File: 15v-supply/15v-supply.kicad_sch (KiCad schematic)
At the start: 29 parts, among them J901 Terminal Block, J902 Terminal Block, P901 120VAC, SW901 SW_SPST, T901 XFORMER, U901 LM7815, U902 LM7915

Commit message: if and log amp routing and 3d model
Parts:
- C901: value (none) -> 0.22u; footprint (none) -> Capacitor_THT:C_Rect_L4.6mm_W5.5mm_P2.50mm_MKS02_FKP02
- D901, D902, D903, D904: Spice_Lib_File 15v-supply-spice\1n5060.lib -> 15v-supply-spice/1n5060.lib
- H901, H902, H903, H905: Spice_Netlist_Enabled (none) -> N; Spice_Primitive (none) -> R
- R901, R902: value (none) -> 2.2k; footprint (none) -> Resistor_THT:R_Axial_DIN0309_L9.0mm_D3.2mm_P12.70mm_Horizontal
- T901: Spice_Lib_File 15v-supply-spice\xformer.lib -> 15v-supply-spice/xformer.lib
- U901, U902: Spice_Lib_File 15v-supply-spice\regulators.lib -> 15v-supply-spice/regulators.lib
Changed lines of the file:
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@@
     (title "Dual Polarity 15V Supply")
     (date "2022-06-16")
-    (rev "0.1")
+    (rev "0.0")
     (company "Andy McCann KA3KAF and Doug McCann KA3KAG")
     (comment 2 "Audiophile's Project Source Book, Fig 7-8")
@@
       (effects (font (size 1.27 1.27)) (justify left))
     )
-    (property "Value" "" (id 1) (at 127 120.6499 0)
-      (effects (font (size 1.27 1.27)) (justify left))
-    )
-    (property "Footprint" "" (id 2) (at 124.46 119.38 0)
+    (property "Value" "2.2k" (id 1) (at 127 120.6499 0)
+      (effects (font (size 1.27 1.27)) (justify left))
+    )
+    (property "Footprint" "Resistor_THT:R_Axial_DIN0309_L9.0mm_D3.2mm_P12.70mm_Horizontal" (id 2) (at 124.46 119.38 0)
       (effects (font (size 1.27 1.27)) hide)
     )
@@
       (effects (font (size 1.27 1.27)) hide)
     )
+    (property "Spice_Primitive" "R" (id 4) (at 39.37 196.85 0)
+      (effects (font (size 1.27 1.27)) hide)
+    )
+    (property "Spice_Netlist_Enabled" "N" (id 5) (at 39.37 196.85 0)
+      (effects (font (size 1.27 1.27)) hide)
+    )
   )
   (symbol (lib_id "Device:C_Small") (at 158.75 40.64 0) (unit 1)
@@
     )
     (property "Datasheet" "~" (id 3) (at 76.2 196.85 0)
+      (effects (font (size 1.27 1.27)) hide)
+    )
+    (property "Spice_Primitive" "R" (id 4) (at 76.2 196.85 0)
+      (effects (font (size 1.27 1.27)) hide)
+    )
+    (property "Spice_Netlist_Enabled" "N" (id 5) (at 76.2 196.85 0)
       (effects (font (size 1.27 1.27)) hide)
     )
@@
       (effects (font (size 1.27 1.27)) hide)
     )
-    (property "Spice_Lib_File" "15v-supply-spice\\1n5060.lib" (id 8) (at 177.8 40.64 0)
+    (property "Spice_Lib_File" "15v-supply-spice/1n5060.lib" (id 8) (at 177.8 40.64 0)
       (effects (font (size 1.27 1.27)) hide)
     )
@@
       (effects (font (size 1.27 1.27)) hide)
     )
-    (property "Spice_Lib_File" "15v-supply-spice\\1n5060.lib" (id 8) (at 140.97 74.93 0)
+    (property "Spice_Lib_File" "15v-supply-spice/1n5060.lib" (id 8) (at 140.97 74.93 0)
       (effects (font (size 1.27 1.27)) hide)
     )
@@
       (effects (font (size 1.27 1.27)) (justify left))
     )
-    (property "Value" "" (id 1) (at 127 152.3999 0)
-      (effects (font (size 1.27 1.27)) (justify left))
-    )
-    (property "Footprint" "" (id 2) (at 124.46 151.13 0)
+    (property "Value" "2.2k" (id 1) (at 127 152.3999 0)
+      (effects (font (size 1.27 1.27)) (justify left))
+    )
+    (property "Footprint" "Resistor_THT:R_Axial_DIN0309_L9.0mm_D3.2mm_P12.70mm_Horizontal" (id 2) (at 124.46 151.13 0)
       (effects (font (size 1.27 1.27)) hide)
     )
@@
       (effects (font (size 1.27 1.27)) hide)
     )
-    (property "Spice_Lib_File" "15v-supply-spice\\xformer.lib" (id 7) (at 87.63 54.61 0)
+    (property "Spice_Lib_File" "15v-supply-spice/xformer.lib" (id 7) (at 87.63 54.61 0)
       (effects (font (size 1.27 1.27)) hide)
     )
@@
       (effects (font (size 1.27 1.27)) hide)
     )
-    (property "Spice_Lib_File" "15v-supply-spice\\1n5060.lib" (id 8) (at 177.8 74.93 0)
+    (property "Spice_Lib_File" "15v-supply-spice/1n5060.lib" (id 8) (at 177.8 74.93 0)
       (effects (font (size 1.27 1.27)) hide)
     )
@@
       (effects (font (size 1.27 1.27)) hide)
     )
+    (property "Spice_Primitive" "R" (id 4) (at 20.32 196.85 0)
+      (effects (font (size 1.27 1.27)) hide)
+    )
+    (property "Spice_Netlist_Enabled" "N" (id 5) (at 20.32 196.85 0)
+      (effects (font (size 1.27 1.27)) hide)
+    )
   )
   (symbol (lib_id "terminal-block:691103110003") (at 121.92 54.61 270) (unit 1)
@@
       (effects (font (size 1.27 1.27)) hide)
     )
-    (property "Spice_Lib_File" "15v-supply-spice\\1n5060.lib" (id 7) (at 140.97 40.64 0)
+    (property "Spice_Lib_File" "15v-supply-spice/1n5060.lib" (id 7) (at 140.97 40.64 0)
       (effects (font (size 1.27 1.27)) hide)
     )
@@
       (effects (font (size 1.27 1.27)) hide)
     )
-    (property "Spice_Lib_File" "15v-supply-spice\\regulators.lib" (id 8) (at 76.2 109.22 0)
+    (property "Spice_Lib_File" "15v-supply-spice/regulators.lib" (id 8) (at 76.2 109.22 0)
       (effects (font (size 1.27 1.27)) hide)
     )
@@
       (effects (font (size 1.27 1.27)) (justify left))
     )
-    (property "Value" "" (id 1) (at 69.85 55.8799 0)
-      (effects (font (size 1.27 1.27)) (justify left))
-    )
-    (property "Footprint" "" (id 2) (at 66.04 54.61 0)
+    (property "Value" "0.22u" (id 1) (at 69.85 55.8799 0)
+      (effects (font (size 1.27 1.27)) (justify left))
+    )
+    (property "Footprint" "Capacitor_THT:C_Rect_L4.6mm_W5.5mm_P2.50mm_MKS02_FKP02" (id 2) (at 66.04 54.61 0)
       (effects (font (size 1.27 1.27)) hide)
     )
@@
       (effects (font (size 1.27 1.27)) hide)
     )
-    (property "Spice_Lib_File" "15v-supply-spice\\regulators.lib" (id 8) (at 76.2 161.29 0)
+    (property "Spice_Lib_File" "15v-supply-spice/regulators.lib" (id 8) (at 76.2 161.29 0)
       (effects (font (size 1.27 1.27)) hide)
     )
@@
       (effects (font (size 1.27 1.27)) hide)
     )
+    (property "Spice_Primitive" "R" (id 4) (at 58.42 196.85 0)
+      (effects (font (size 1.27 1.27)) hide)
+    )
+    (property "Spice_Netlist_Enabled" "N" (id 5) (at 58.42 196.85 0)
+      (effects (font (size 1.27 1.27)) hide)
+    )

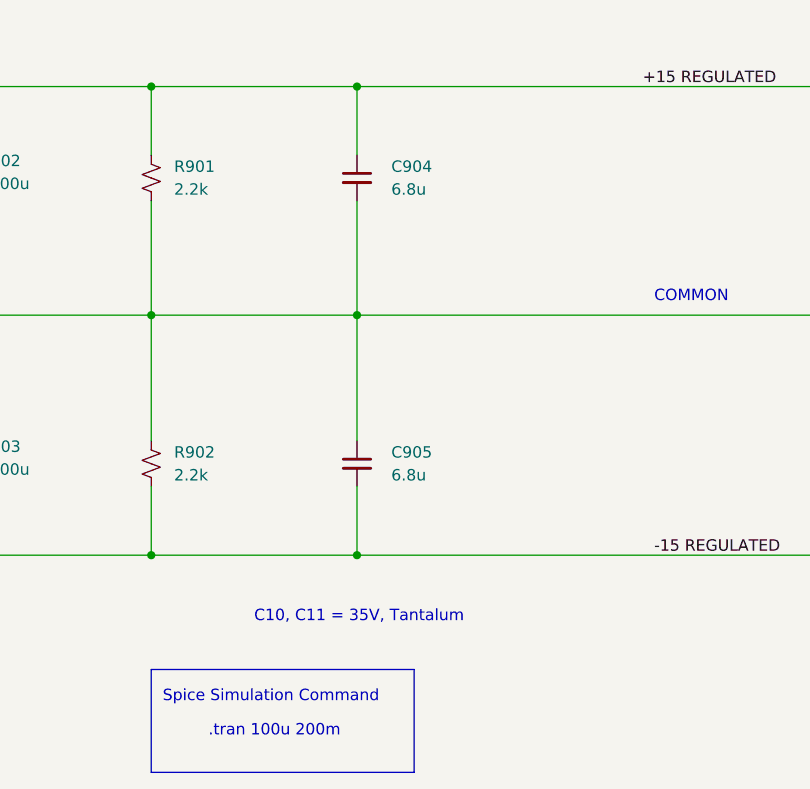
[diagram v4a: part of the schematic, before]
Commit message: Improvements to if and log amp
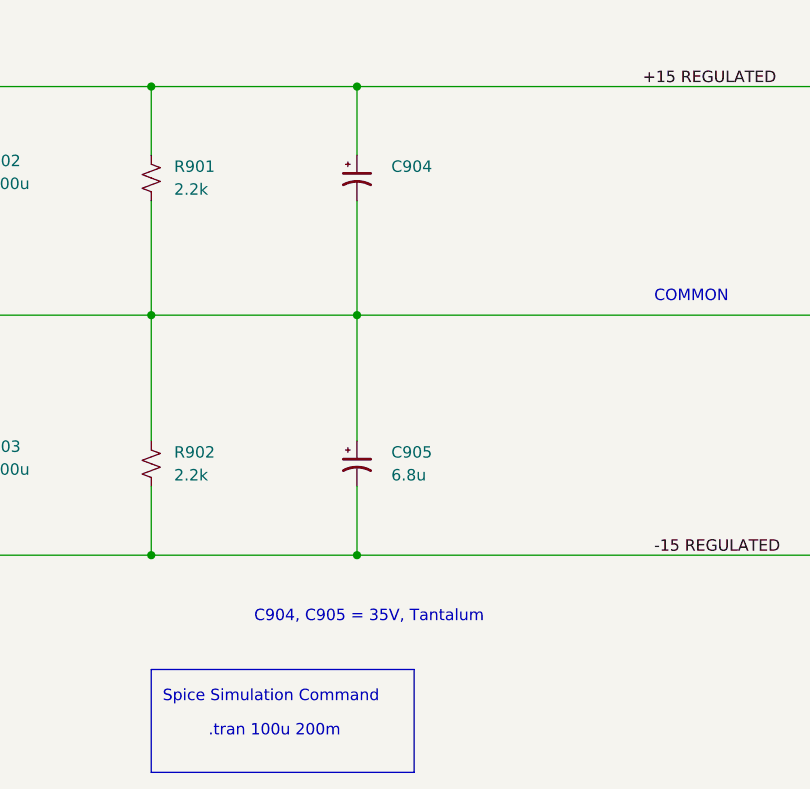
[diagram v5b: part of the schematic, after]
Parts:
- C904: value 6.8u -> (none); footprint Capacitor_THT:CP_Radial_D5.0mm_P2.50mm -> (none); symbol Device:C_Small -> Device:C_Polarized_Small_US
- C905: symbol Device:C_Small -> Device:C_Polarized_Small_US
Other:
- note added: "C904, C905 = 35V, Tantalum"
- note removed: "C10, C11 = 35V, Tantalum"
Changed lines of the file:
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@@
     (effects (font (size 1.27 1.27)) (justify left bottom))
   )
-  (text "C10, C11 = 35V, Tantalum" (at 135.89 168.91 0)
+  (text "C904, C905 = 35V, Tantalum" (at 135.89 168.91 0)
     (effects (font (size 1.27 1.27)) (justify left bottom))
   )
@@
     (pin "2")
   )
-  (symbol (lib_id "Device:C_Small") (at 147.32 151.13 0) (unit 1)
+  (symbol (lib_id "Device:C_Polarized_Small_US") (at 147.32 151.13 0) (unit 1)
     (in_bom yes) (on_board yes) (fields_autoplaced)
     (property "Reference" "C905" (id 0) (at 151.13 149.8599 0)
@@
       (effects (font (size 1.27 1.27)) hide)
     )
-    (property "Datasheet" "https://datasheets.kyocera-avx.com/tap.pdf" (id 3) (at 147.32 151.13 0)
-      (effects (font (size 1.27 1.27)) hide)
-    )
-    (pin "1")
-    (pin "2")
-  )
-  (symbol (lib_id "Device:C_Small") (at 147.32 119.38 0) (unit 1)
+    (property "Datasheet" "~" (id 3) (at 147.32 151.13 0)
+      (effects (font (size 1.27 1.27)) hide)
+    )
+    (pin "1")
+    (pin "2")
+  )
+  (symbol (lib_id "Device:C_Polarized_Small_US") (at 147.32 119.38 0) (unit 1)
     (in_bom yes) (on_board yes) (fields_autoplaced)
     (property "Reference" "C904" (id 0) (at 151.13 118.1099 0)
       (effects (font (size 1.27 1.27)) (justify left))
     )
-    (property "Value" "6.8u" (id 1) (at 151.13 120.6499 0)
-      (effects (font (size 1.27 1.27)) (justify left))
-    )
-    (property "Footprint" "Capacitor_THT:CP_Radial_D5.0mm_P2.50mm" (id 2) (at 147.32 119.38 0)
-      (effects (font (size 1.27 1.27)) hide)
-    )
-    (property "Datasheet" "https://datasheets.kyocera-avx.com/tap.pdf" (id 3) (at 147.32 119.38 0)
-      (effects (font (size 1.27 1.27)) hide)
-    )
+    (property "Value" "" (id 1) (at 151.13 120.6499 0)
+      (effects (font (size 1.27 1.27)) (justify left))
+    )
+    (property "Footprint" "" (id 2) (at 147.32 119.38 0)
+      (effects (font (size 1.27 1.27)) hide)
+    )
+    (property "Datasheet" "~" (id 3) (at 147.32 119.38 0)
+      (effects (font (size 1.27 1.27)) hide)
+    )

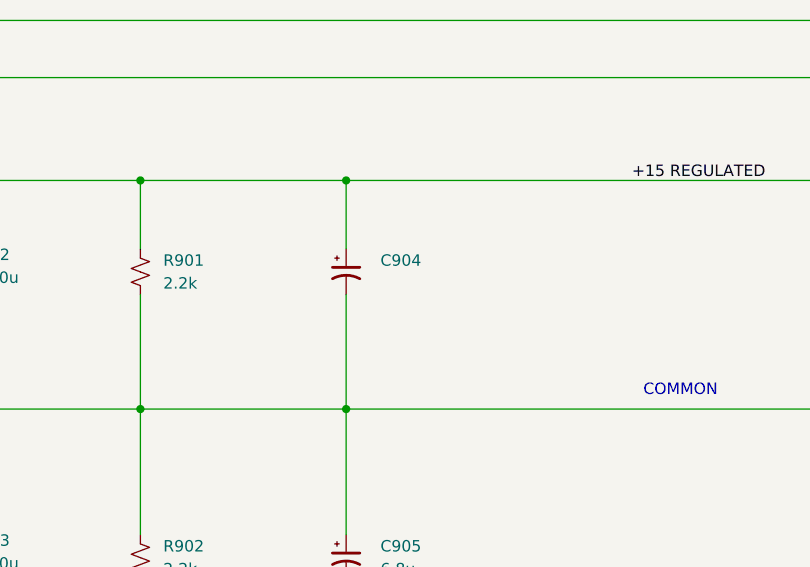
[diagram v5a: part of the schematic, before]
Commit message: updates to 15v supply and if and log amp boards so boards can be sent to fab
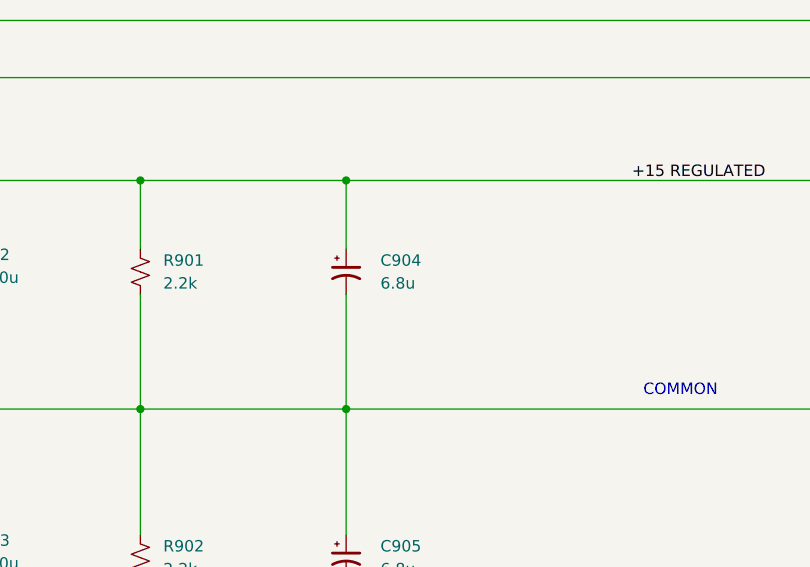
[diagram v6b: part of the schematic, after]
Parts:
- C904: value (none) -> 6.8u; footprint (none) -> Capacitor_THT:CP_Radial_D5.0mm_P2.50mm
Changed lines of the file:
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@@
       (effects (font (size 1.27 1.27)) (justify left))
     )
-    (property "Value" "" (id 1) (at 151.13 120.6499 0)
+    (property "Value" "6.8u" (id 1) (at 151.13 120.6499 0)
       (effects (font (size 1.27 1.27)) (justify left))
     )
-    (property "Footprint" "" (id 2) (at 147.32 119.38 0)
+    (property "Footprint" "Capacitor_THT:CP_Radial_D5.0mm_P2.50mm" (id 2) (at 147.32 119.38 0)
       (effects (font (size 1.27 1.27)) hide)
     )

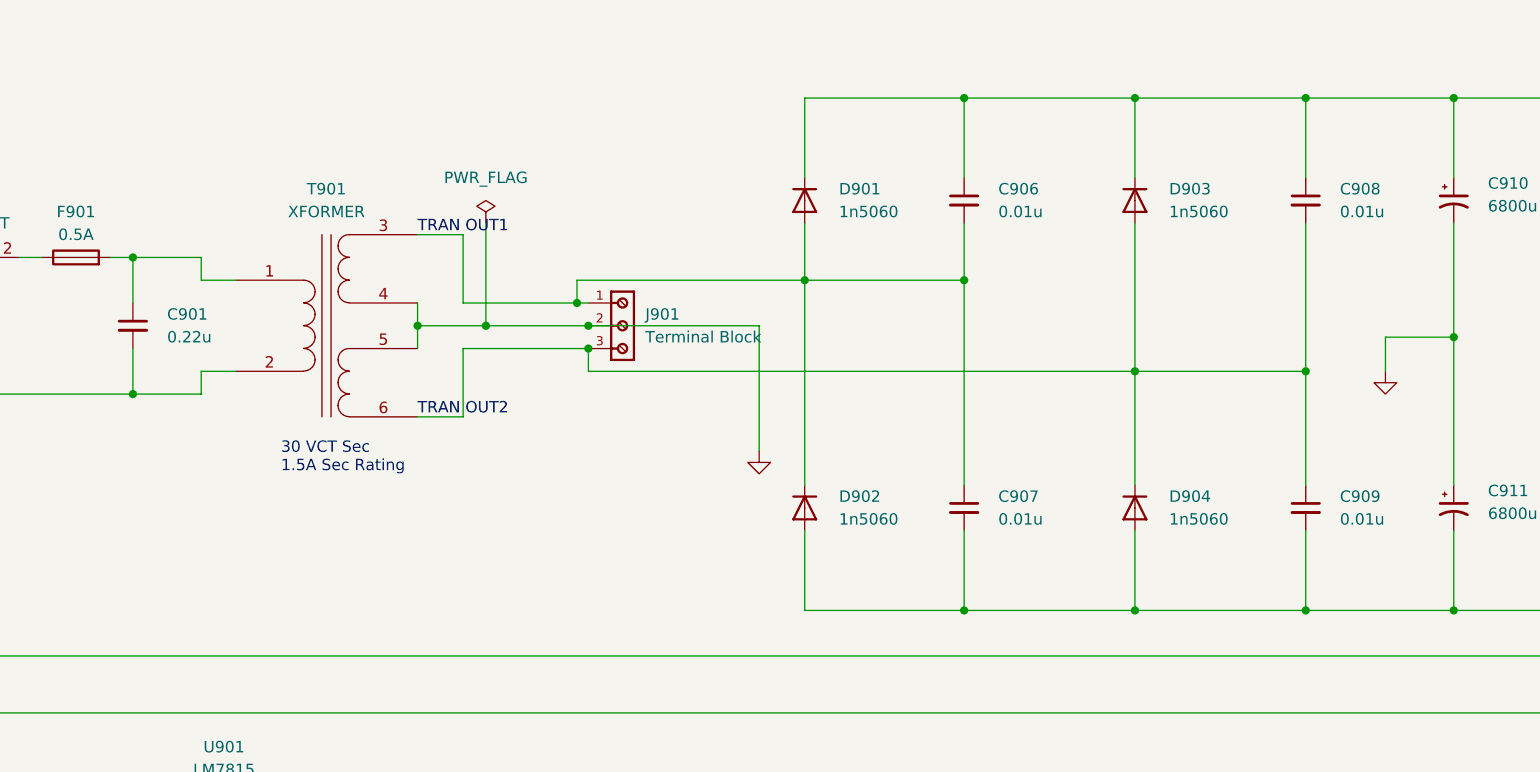
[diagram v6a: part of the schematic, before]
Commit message: 15v-supply changes
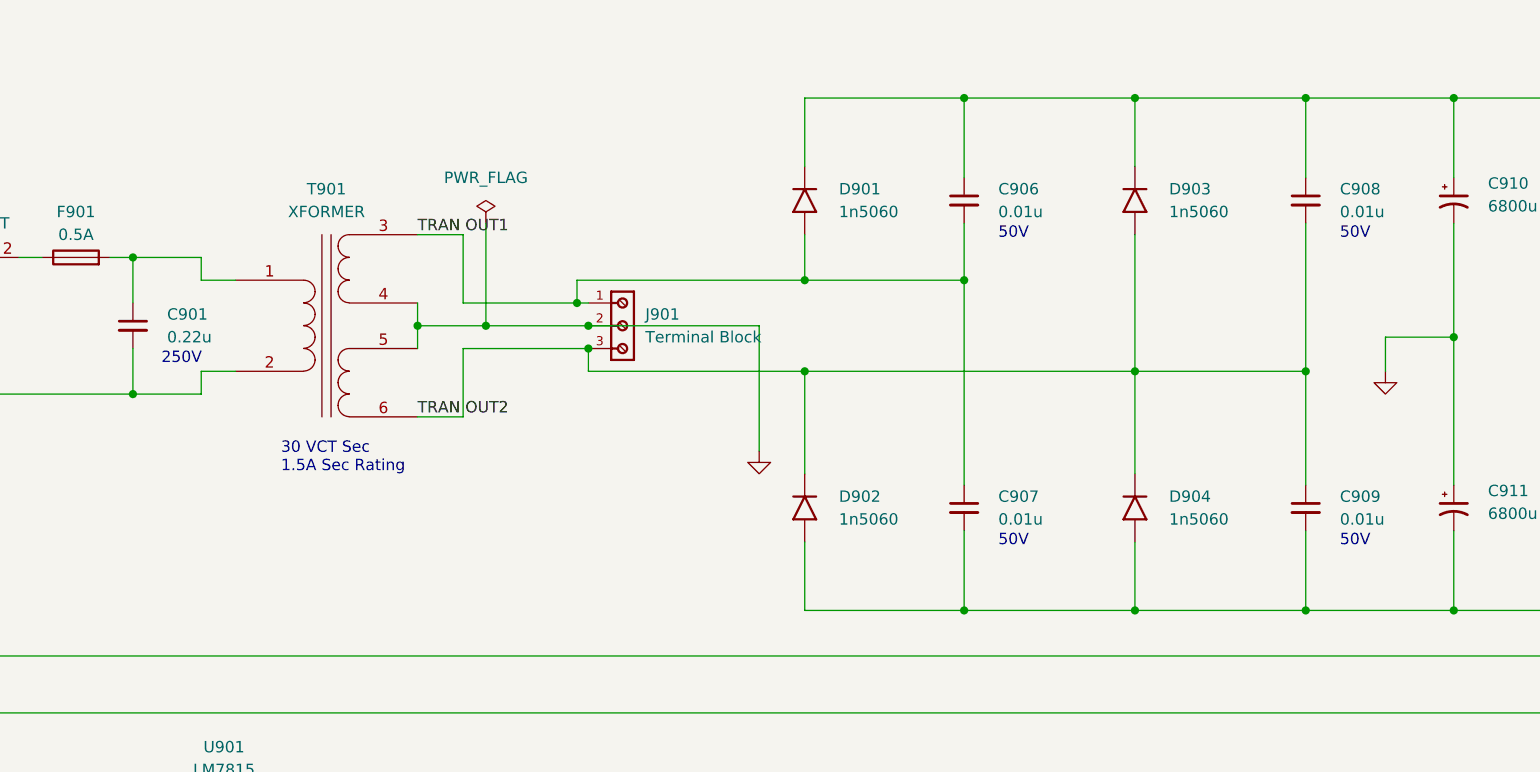
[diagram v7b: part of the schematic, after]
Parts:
- D901, D902, D903, D904: Spice_Node_Sequence (none) -> 2 1
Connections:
- net 7815 IN: now also D901.1 (Cathode), D903.1 (Cathode); no longer D901.2 (Anode), D903.2 (Anode)
- net 7915 IN: now also D902.2 (Anode), D904.2 (Anode); no longer D902.1 (Cathode), D904.1 (Cathode)
- net TRAN OUT1: now also D901.2 (Anode); no longer D901.1 (Cathode), D902.2 (Anode)
- net TRAN OUT2: now also D902.1 (Cathode), D903.2 (Anode), D904.1 (Cathode); no longer D903.1 (Cathode), D904.2 (Anode)
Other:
- note added: "250V"
- note added: "50V"

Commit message: 15v-supply update
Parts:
- C904, C905: footprint Capacitor_THT:CP_Radial_D5.0mm_P2.50mm -> Capacitor_THT:CP_Radial_D8.0mm_P3.50mm
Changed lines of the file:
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@@
       (effects (font (size 1.27 1.27)) hide)
     )
-    (property "Spice_Node_Sequence" "2 1" (id 8) (at 177.8 40.64 0)
+    (property "Spice_Node_Sequence" "2 1" (id 9) (at 177.8 40.64 0)
       (effects (font (size 1.27 1.27)) hide)
     )
@@
       (effects (font (size 1.27 1.27)) hide)
     )
-    (property "Spice_Node_Sequence" "2 1" (id 8) (at 140.97 74.93 0)
+    (property "Spice_Node_Sequence" "2 1" (id 9) (at 140.97 74.93 0)
       (effects (font (size 1.27 1.27)) hide)
     )
@@
       (effects (font (size 1.27 1.27)) hide)
     )
-    (property "Spice_Node_Sequence" "2 1" (id 8) (at 177.8 74.93 0)
+    (property "Spice_Node_Sequence" "2 1" (id 9) (at 177.8 74.93 0)
       (effects (font (size 1.27 1.27)) hide)
     )
@@
       (effects (font (size 1.27 1.27)) (justify left))
     )
-    (property "Footprint" "Capacitor_THT:CP_Radial_D5.0mm_P2.50mm" (id 2) (at 147.32 151.13 0)
+    (property "Footprint" "Capacitor_THT:CP_Radial_D8.0mm_P3.50mm" (id 2) (at 147.32 151.13 0)
       (effects (font (size 1.27 1.27)) hide)
     )
@@
       (effects (font (size 1.27 1.27)) (justify left))
     )
-    (property "Footprint" "Capacitor_THT:CP_Radial_D5.0mm_P2.50mm" (id 2) (at 147.32 119.38 0)
+    (property "Footprint" "Capacitor_THT:CP_Radial_D8.0mm_P3.50mm" (id 2) (at 147.32 119.38 0)
       (effects (font (size 1.27 1.27)) hide)
     )
@@
     )
     (path "/a9b19d95-a284-401d-82af-2e99e16425cc"
-      (reference "C904") (unit 1) (value "6.8u") (footprint "Capacitor_THT:CP_Radial_D5.0mm_P2.50mm")
+      (reference "C904") (unit 1) (value "6.8u") (footprint "Capacitor_THT:CP_Radial_D8.0mm_P3.50mm")
     )
     (path "/a7f04f54-110b-431c-a1d7-3b45826c09eb"
-      (reference "C905") (unit 1) (value "6.8u") (footprint "Capacitor_THT:CP_Radial_D5.0mm_P2.50mm")
+      (reference "C905") (unit 1) (value "6.8u") (footprint "Capacitor_THT:CP_Radial_D8.0mm_P3.50mm")
     )
     (path "/0c90dd19-5c42-4dc8-a385-412fb3a1e3c2"
